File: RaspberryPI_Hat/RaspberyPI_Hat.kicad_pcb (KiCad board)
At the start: 2 copper layers, 65 x 56 mm, 37 parts, among them P1 Raspberry_PI, P3 CONN_01X03, P4 RAS-05-15, P5 LCD_16x2, Q1 BC817, Q2 BC817, Q3 BC817, SW1 SW_PUSH, U1 CAT24C32WI-GT3, U2 TSOP382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

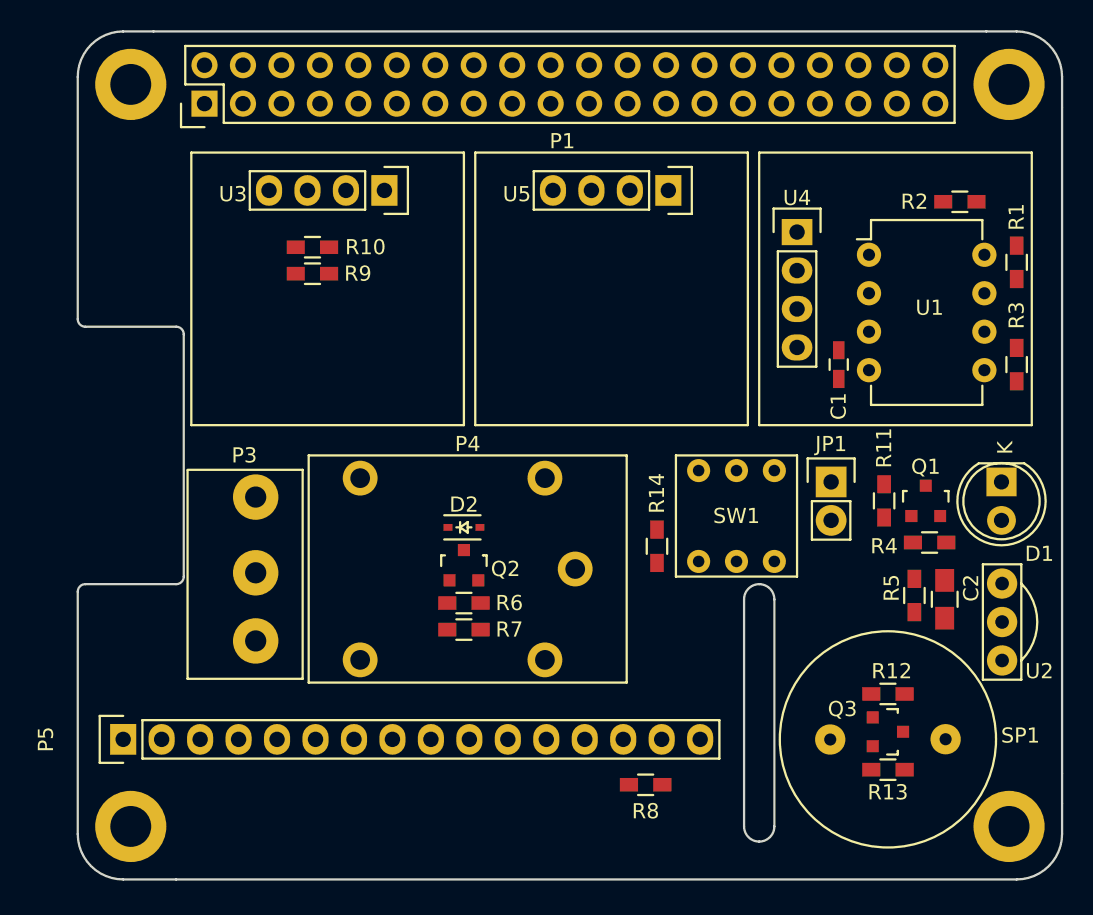
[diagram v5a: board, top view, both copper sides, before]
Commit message: Добавен RG LED оправени корпуси
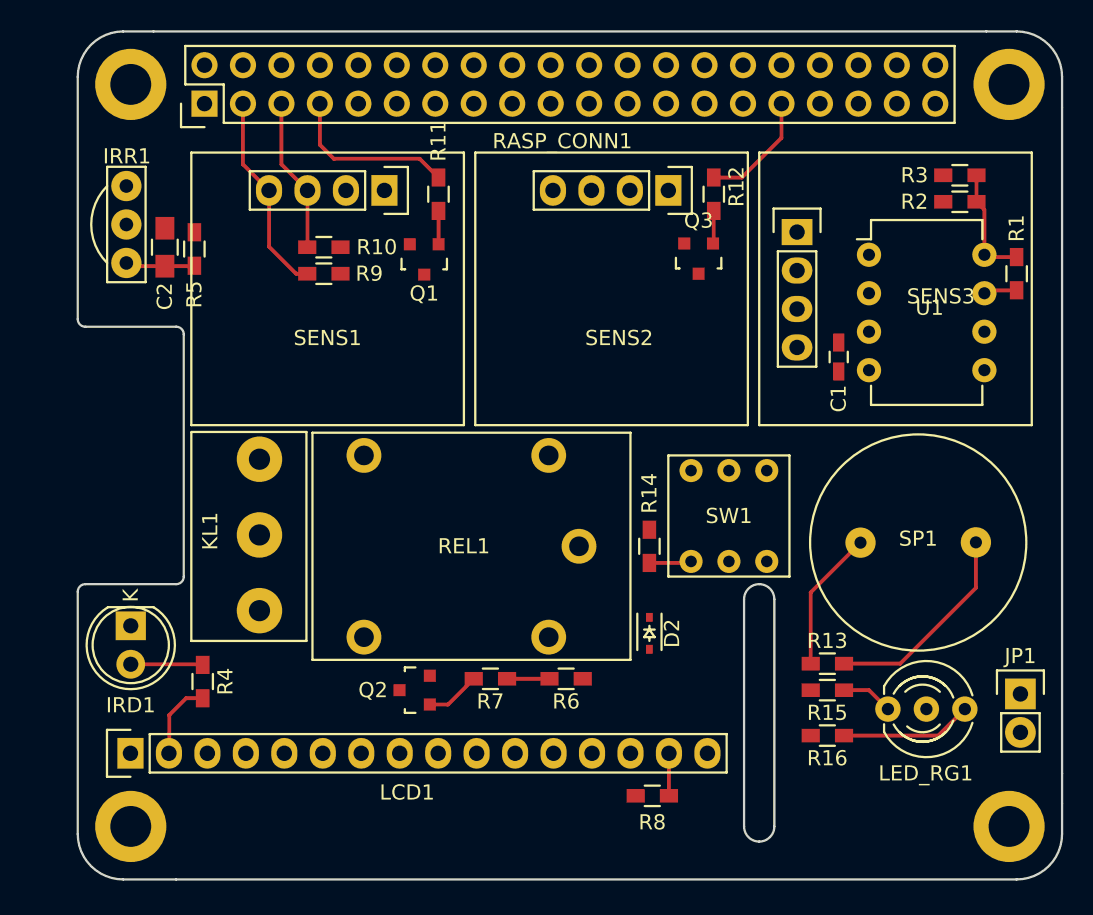
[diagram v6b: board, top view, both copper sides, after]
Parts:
- removed P3: CONN_01X03, myfootprint:KLEMA_1x3
- removed P4: RAS-05-15, myfootprint:RAS-05-15
- removed P5: LCD_16x2, Pin_Headers:Pin_Header_Straight_1x16
- removed U4: I2C_SENS_1, myfootprint:I2C_SENS_1
- added KL1: CONN_01X03, myfootprint:KLEMA_1x3, F.Cu at (113.5, 96.8)
- added LCD1: LCD_16x2, Pin_Headers:Pin_Header_Straight_1x16, F.Cu at (101.5, 116.3)
- added LED_RG1: Led_x2, LEDs:LED-5MM-3, F.Cu at (151.5, 113.3)
- added R15: 220, Resistors_SMD:R_0603_HandSoldering, F.Cu at (147.5, 112.1)
- added R16: 220, Resistors_SMD:R_0603_HandSoldering, F.Cu at (147.5, 115.1)
- added REL1: RAS-05-15, myfootprint:RAS-05-15, F.Cu at (119.0, 95.1)
- added SENS3: I2C_SENS_1, myfootprint:I2C_SENS_1, F.Cu at (143.0, 76.6)
- IRD1: renamed from D1; value TSAL4600 -> L-934F3BT
- IRR1: renamed from U2; value TSOP382 -> TSOP34838
- SP1: value BUZZER -> MCKPI-G1410-3668
- moved IRR1 58.9 mm to (103.8, 81.3), turned to 270 degrees
- moved IRD1 58.3 mm to (101.5, 107.8)
- moved C2 56.5 mm to (103.8, 82.8), turned to 90 degrees
- moved R5 52.8 mm to (105.7, 83.0)
- moved R4 48.9 mm to (106.2, 111.5), turned to 90 degrees
- moved Q1 36.8 mm to (120.9, 83.7), turned to 180 degrees
- moved R11 35.7 mm to (121.8, 79.3)
- moved R12 34.9 mm to (140.0, 79.3), turned to 90 degrees
- moved Q3 33.7 mm to (139.0, 83.6), turned to 180 degrees
- moved JP1 18.8 mm to (160.2, 112.3)
- moved D2 14.1 mm to (135.8, 108.3), turned to 270 degrees
- moved SP1 13.2 mm to (153.5, 102.3)
- moved R3 13.1 mm to (156.2, 78.1), turned to 180 degrees
- moved Q2 8.87 mm to (120.2, 112.1), turned to 90 degrees
- moved R6 8.40 mm to (130.2, 111.3), turned to 180 degrees
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- renumbered P1 to RASP_CONN1, U3 to SENS1, U5 to SENS2
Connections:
- IRD1 pad 2: Net-(D1-Pad2) -> Net-(IRD1-Pad2)
- IRR1 pad 1: Net-(P1-Pad37) -> Net-(IRR1-Pad1)
- R4 pad 1: Net-(D1-Pad2) -> +5V
- R4 pad 2: +5V -> Net-(IRD1-Pad2)
- RASP_CONN1 pad 33: Net-(P1-Pad33) -> /LED1
- RASP_CONN1 pad 36: Net-(P1-Pad36) -> /LED2
- RASP_CONN1 pad 37: Net-(P1-Pad37) -> Net-(RASP_CONN1-Pad37)
- RASP_CONN1 pad 40: Net-(P1-Pad40) -> Net-(RASP_CONN1-Pad40)
- SW1 pad 1: Net-(P1-Pad37) -> Net-(RASP_CONN1-Pad40)
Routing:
- net +5V: track 0.00 -> 14.1 mm
- net Net-(Q3-Pad3): track 0.00 -> 13.8 mm
- net Net-(R9-Pad2): track 0.00 -> 13.4 mm
- net Net-(R11-Pad2): track 0.00 -> 11.4 mm
- net Net-(R10-Pad2): track 0.00 -> 10.2 mm
- net Net-(LED_RG1-Pad3): track 0.00 -> 8.70 mm
- net +3V3: track 0.00 -> 8.51 mm
- net Net-(R12-Pad2): track 0.00 -> 7.82 mm
- net Net-(IRD1-Pad2): track 0.00 -> 4.77 mm
- net Net-(C2-Pad1): track 0.00 -> 4.59 mm
- net Net-(Q2-Pad1): track 0.00 -> 3.60 mm
- net Net-(LED_RG1-Pad1): track 0.00 -> 3.42 mm
- net Net-(LCD1-Pad15): track 0.00 -> 3.24 mm
- net Net-(R6-Pad2): track 0.00 -> 2.80 mm
- net Net-(R14-Pad1): track 0.00 -> 2.79 mm
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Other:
- net class Default: clearance 0.2 -> 0.254; trace_width 0.25 -> 0.254
- rule trace_clearance: 0.2 -> 0.254

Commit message: Започнато трасиране на платка
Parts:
- R11, R12: value 2.2K -> 12K
- R14: value 470 -> 10K
- R4: value 100 -> 130
- R6: value 10K -> 22K
- R7: value 2.2K -> 10K
- moved R13 17.1 mm to (145.3, 93.4)
- moved C1 15.2 mm to (158.8, 79.1), turned to 90 degrees
- moved R8 11.8 mm to (138.5, 107.6), turned to 90 degrees
- moved R16 10.0 mm to (157.1, 112.2), turned to 270 degrees
- moved R6 5.02 mm to (125.2, 111.6)
- moved R9 3.93 mm to (110.6, 83.1), turned to 90 degrees
- moved LED_RG1 2.25 mm to (149.2, 113.3)
- moved R7 2.00 mm to (125.2, 113.3)
- moved U1 1.38 mm to (149.0, 83.9)
- moved R14 1.37 mm to (135.9, 101.2)
- moved SW1 1.24 mm to (141.3, 99.4)
- moved R1 1.23 mm to (158.8, 85.0)
- moved R10 1.10 mm to (113.2, 83.1), turned to 90 degrees
- moved R15 1.01 mm to (146.5, 112.2), turned to 270 degrees
- moved Q2 0.86 mm to (119.4, 112.3)
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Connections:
- R6 pad 2: Net-(R6-Pad2) -> Net-(Q2-Pad1)
- R7 pad 2: Net-(R6-Pad2) -> Net-(R7-Pad2)
- RASP_CONN1 pad 12: Net-(RASP_CONN1-Pad12) -> Net-(IRR1-Pad1)
- RASP_CONN1 pad 13: /D6 -> Net-(RASP_CONN1-Pad13)
- RASP_CONN1 pad 31: Net-(R12-Pad2) -> /LED2
- RASP_CONN1 pad 32: Net-(RASP_CONN1-Pad32) -> Net-(R12-Pad2)
- RASP_CONN1 pad 35: Net-(R6-Pad2) -> Net-(R7-Pad2)
- RASP_CONN1 pad 36: /LED2 -> Net-(RASP_CONN1-Pad36)
- RASP_CONN1 pad 38: (no net) -> Net-(RASP_CONN1-Pad38)
- RASP_CONN1 pad 40: Net-(RASP_CONN1-Pad40) -> /D6
- REL1 pad 1: Net-(KL1-Pad3) -> Net-(KL1-Pad2)
- REL1 pad 3: Net-(KL1-Pad2) -> Net-(KL1-Pad3)
- SW1 pad 1: Net-(RASP_CONN1-Pad40) -> Net-(RASP_CONN1-Pad13)
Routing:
- net +5V: track 14.1 -> 164.7 mm
- net +3V3: track 8.51 -> 82.5 mm, vias 0 -> 1
- net /LED2: track 0.00 -> 49.2 mm
- net Net-(R9-Pad2): track 13.4 -> 56.6 mm, vias 0 -> 1
- net Net-(R10-Pad2): track 10.2 -> 52.8 mm
- net /LED1: track 0.00 -> 42.0 mm
- net Net-(IRD1-Pad1): track 0.00 -> 36.9 mm
- net Net-(JP1-Pad1): track 2.21 -> 29.3 mm
- net Net-(KL1-Pad1): track 0.00 -> 26.2 mm
- net Net-(D2-Pad2): track 0.00 -> 19.8 mm
- net Net-(R3-Pad2): track 0.00 -> 16.4 mm
- net Net-(KL1-Pad2): track 0.00 -> 11.3 mm
- net Net-(R2-Pad2): track 0.00 -> 9.75 mm
- net Net-(Q3-Pad3): track 13.8 -> 22.7 mm
- net Net-(KL1-Pad3): track 0.00 -> 7.62 mm
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- added copper zone on B.Cu, net GND
- added copper zone on F.Cu, net GND
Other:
- net class Default: trace_width 0.254 -> 0.5; via_dia 0.6 -> 0.85
- net class VCC added: clearance 0.254, trace_width 1.5, via_dia 0.85, via_drill 0.4
- rule trace_min: 0.2 -> 0.254
- rule via_min_drill: 0.3 -> 0.35
- rule via_min_size: 0.4 -> 0.7

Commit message: Първи вариант PCB
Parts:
- moved R6 21.5 mm to (131.6, 91.1)
- moved Q2 21.1 mm to (126.5, 92.5)
- moved R7 20.8 mm to (131.6, 93.5)
- moved R11 11.4 mm to (116.4, 89.3), turned to 0 degrees
- moved Q1 11.0 mm to (112.2, 90.3)
- moved R13 10.7 mm to (143.4, 103.9)
- moved R12 5.42 mm to (137.6, 84.2)
- moved Q3 4.45 mm to (134.7, 84.5)
- moved R4 4.07 mm to (102.6, 113.3), turned to 180 degrees
- moved R14 3.75 mm to (136.0, 97.5)
- moved R8 1.90 mm to (138.4, 105.7)
- moved D2 1.88 mm to (135.9, 105.7)
- moved SP1 1.19 mm to (154.7, 102.5), turned to 180 degrees
- moved JP1 0.59 mm to (159.8, 111.9)
- moved SW1 0.52 mm to (141.3, 98.9)
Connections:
- RASP_CONN1 pad 11: /D5 -> /EN
- RASP_CONN1 pad 13: Net-(RASP_CONN1-Pad13) -> /D4
- RASP_CONN1 pad 15: /D7 -> /D5
- RASP_CONN1 pad 16: /D4 -> Net-(RASP_CONN1-Pad16)
- RASP_CONN1 pad 18: /EN -> Net-(RASP_CONN1-Pad18)
- RASP_CONN1 pad 19: Net-(RASP_CONN1-Pad19) -> /D6
- RASP_CONN1 pad 21: Net-(RASP_CONN1-Pad21) -> /D7
- RASP_CONN1 pad 22: /RS -> Net-(RASP_CONN1-Pad22)
- RASP_CONN1 pad 29: Net-(RASP_CONN1-Pad29) -> Net-(R12-Pad2)
- RASP_CONN1 pad 31: /LED2 -> Net-(R7-Pad2)
- RASP_CONN1 pad 32: Net-(R12-Pad2) -> Net-(RASP_CONN1-Pad32)
- RASP_CONN1 pad 33: /LED1 -> /LED2
- RASP_CONN1 pad 35: Net-(R7-Pad2) -> /LED1
- RASP_CONN1 pad 40: /D6 -> Net-(RASP_CONN1-Pad40)
- RASP_CONN1 pad 7: Net-(R11-Pad2) -> /RS
- RASP_CONN1 pad 8: Net-(RASP_CONN1-Pad8) -> Net-(R11-Pad2)
- SW1 pad 1: Net-(RASP_CONN1-Pad13) -> Net-(RASP_CONN1-Pad23)
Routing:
- net /D7: track 0.00 -> 49.9 mm
- net /D6: track 0.00 -> 48.8 mm
- net /RS: track 0.00 -> 47.1 mm, vias 0 -> 2
- net /D5: track 0.00 -> 46.5 mm
- net Net-(R2-Pad2): track 9.75 -> 55.6 mm
- net /EN: track 0.00 -> 45.7 mm
- net /D4: track 0.00 -> 45.2 mm
- net Net-(RASP_CONN1-Pad23): track 0.00 -> 32.0 mm
- net Net-(IRR1-Pad1): track 0.00 -> 31.3 mm
- net Net-(R7-Pad2): track 0.00 -> 31.0 mm, vias 0 -> 2
- net +3V3: track 82.5 -> 104.7 mm, vias 1 -> 0
- net Net-(R3-Pad2): track 16.4 -> 35.3 mm, vias 0 -> 1
- net Net-(Q3-Pad3): track 22.7 -> 40.2 mm, vias 0 -> 4
- net Net-(IRD1-Pad1): track 36.9 -> 24.4 mm, vias 0 -> 1
- net /LED2: track 49.2 -> 38.1 mm
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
